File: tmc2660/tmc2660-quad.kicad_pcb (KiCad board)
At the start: 4 copper layers, 125 x 40 mm, 81 parts, among them J1 Power, J100 0R, J2 DataIn, J200 0R, J300 0R, J400 0R, M0 Mount, M1 Mount, M100 Mount, M101 Mount, M200 Mount, M201 Mount, M300 Mount, M301 Mount, M400 Mount, M401 Mount, P100 Motor, P200 Motor, P300 Motor, P400 Motor, U100 TMC2660, U200 TMC2660, U300 TMC2660, U400 TMC2660

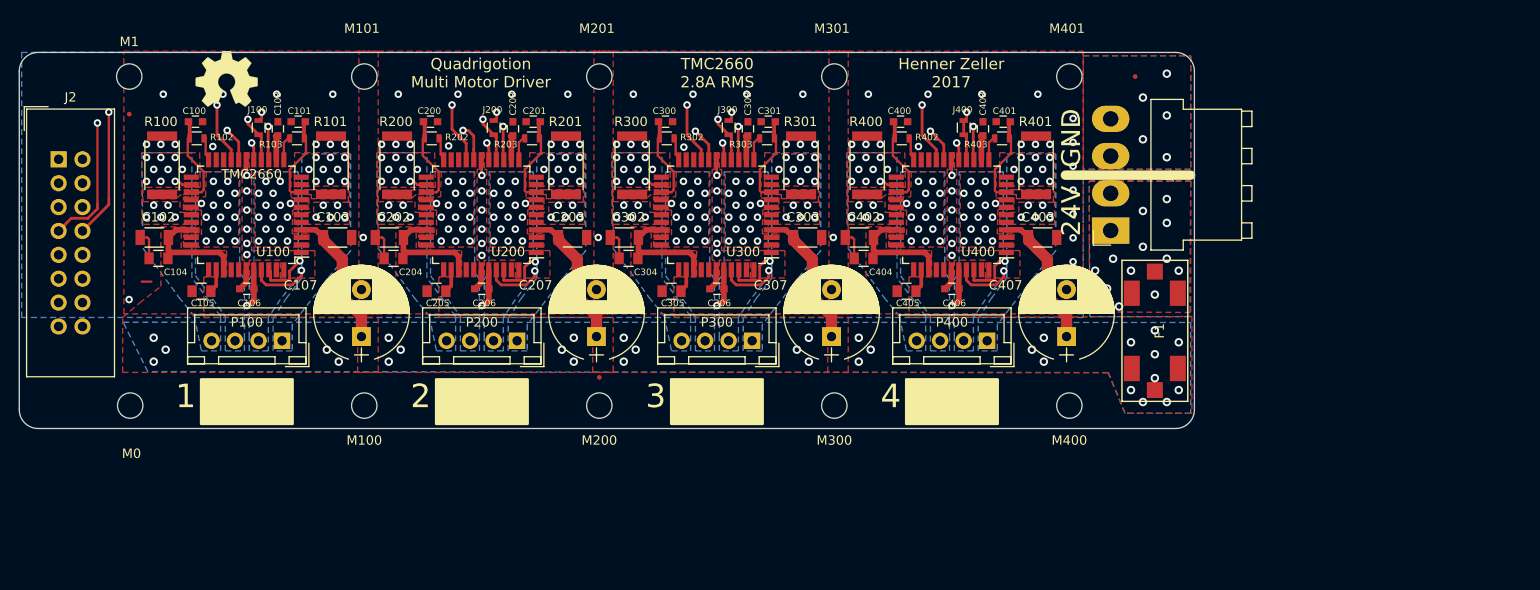
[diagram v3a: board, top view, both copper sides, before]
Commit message: Update tmc2660-quad with new template.
o Start out with a tmc2660-quad-baseline that is filled
  in with zones and tracks from the template.
o The separation from baseline and template allows faster
  updates later.
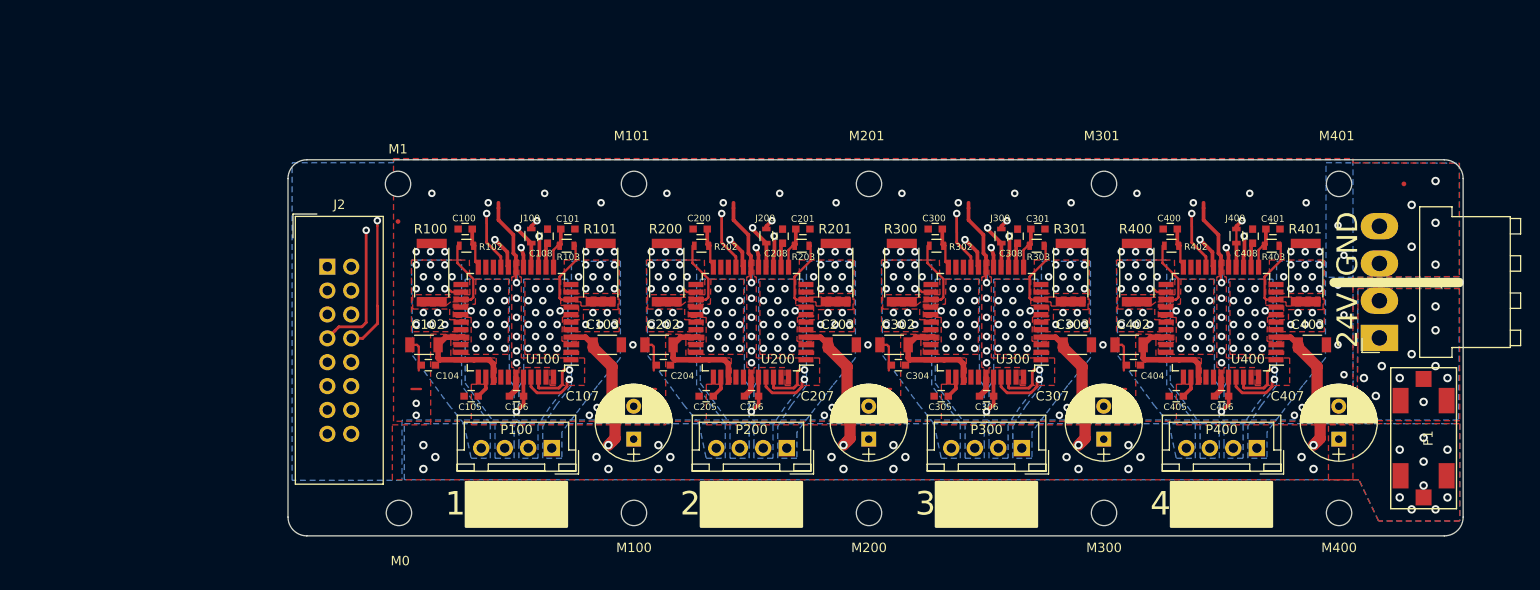
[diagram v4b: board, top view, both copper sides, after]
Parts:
- removed the REF** at (121.3, 83.1)
- removed REF***: OSHW-Symbol_6.7x6mm_SilkScreen, Symbols:OSHW-Symbol_6.7x6mm_SilkScreen
- C104, C105, C204, C205, C304, C305, C404, C405: footprint Capacitors_SMD:C_0805 -> Capacitors_SMD:C_0603
- C107, C207, C307, C407: value 100u -> 180u; footprint Capacitors_THT:CP_Radial_D10.0mm_P5.00mm -> Capacitors_THT:CP_Radial_D8.0mm_P3.50mm
- moved J100 31.2 mm to (114.1, 68.0)
- moved J200 31.2 mm to (139.1, 68.0)
- moved J300 31.2 mm to (164.1, 68.0)
- moved J400 31.2 mm to (189.1, 68.0)
- moved C107 30.9 mm to (125.0, 89.7)
- moved C207 30.9 mm to (150.0, 89.7)
- moved C307 30.9 mm to (175.0, 89.7)
- moved C407 30.9 mm to (200.0, 89.7)
- moved C103 30.9 mm to (122.2, 79.6)
- moved C106 30.9 mm to (112.5, 85.1)
- moved C206 30.9 mm to (137.5, 85.1)
- moved C306 30.9 mm to (162.5, 85.1)
- moved C402 30.9 mm to (177.7, 79.6)
- moved C406 30.9 mm to (187.5, 85.1)
- moved M100 30.9 mm to (125.0, 97.5)
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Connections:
- net Net-(C105-Pad2) renamed /TMC2660-100/VHS
- net Net-(C205-Pad2) renamed /TMC2660-200/VHS
- net Net-(C305-Pad2) renamed /TMC2660-300/VHS
- net Net-(C405-Pad2) renamed /TMC2660-400/VHS
- C100 pad 1: /TMC2660-100/BRB -> GND
- C100 pad 2: GND -> Net-(C100-Pad2)
- C101 pad 1: GND -> Net-(C101-Pad1)
- C101 pad 2: /TMC2660-100/BRA -> GND
- C200 pad 1: /TMC2660-200/BRB -> GND
- C200 pad 2: GND -> Net-(C200-Pad2)
- C201 pad 1: GND -> Net-(C201-Pad1)
- C201 pad 2: /TMC2660-200/BRA -> GND
- C300 pad 1: /TMC2660-300/BRB -> GND
- C300 pad 2: GND -> Net-(C300-Pad2)
- C301 pad 1: GND -> Net-(C301-Pad1)
- C301 pad 2: /TMC2660-300/BRA -> GND
- C400 pad 1: /TMC2660-400/BRB -> GND
- C400 pad 2: GND -> Net-(C400-Pad2)
- C401 pad 1: GND -> Net-(C401-Pad1)
- C401 pad 2: /TMC2660-400/BRA -> GND
- R102 pad 2: Net-(R102-Pad2) -> Net-(C100-Pad2)
- R103 pad 1: Net-(R103-Pad1) -> Net-(C101-Pad1)
- R202 pad 2: Net-(R202-Pad2) -> Net-(C200-Pad2)
- R203 pad 1: Net-(R203-Pad1) -> Net-(C201-Pad1)
- R302 pad 2: Net-(R302-Pad2) -> Net-(C300-Pad2)
- R303 pad 1: Net-(R303-Pad1) -> Net-(C301-Pad1)
- R402 pad 2: Net-(R402-Pad2) -> Net-(C400-Pad2)
- R403 pad 1: Net-(R403-Pad1) -> Net-(C401-Pad1)
- U100 pad 12: Net-(R103-Pad1) -> Net-(C101-Pad1)
- U100 pad 22: Net-(R102-Pad2) -> Net-(C100-Pad2)
- U200 pad 12: Net-(R203-Pad1) -> Net-(C201-Pad1)
- U200 pad 22: Net-(R202-Pad2) -> Net-(C200-Pad2)
- U300 pad 12: Net-(R303-Pad1) -> Net-(C301-Pad1)
- U300 pad 22: Net-(R302-Pad2) -> Net-(C300-Pad2)
- U400 pad 12: Net-(R403-Pad1) -> Net-(C401-Pad1)
- U400 pad 22: Net-(R402-Pad2) -> Net-(C400-Pad2)
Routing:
- net GND: track 39.3 -> 71.2 mm, vias 102 -> 98
- net GLOBAL_MOSI: track 113.7 -> 129.7 mm
- net SCLK: track 106.4 -> 121.0 mm
- net ~ENABLE: track 123.2 -> 133.6 mm
- net CS: track 114.9 -> 124.7 mm
- net Net-(C401-Pad1): track 0.00 -> 4.59 mm
- net Net-(C301-Pad1): track 0.00 -> 4.59 mm
- net Net-(C201-Pad1): track 0.00 -> 4.59 mm
- net Net-(C101-Pad1): track 0.00 -> 4.59 mm
- net Net-(C400-Pad2): track 0.00 -> 4.54 mm
- net Net-(C300-Pad2): track 0.00 -> 4.54 mm
- net Net-(C200-Pad2): track 0.00 -> 4.54 mm
- net Net-(C100-Pad2): track 0.00 -> 4.54 mm
- net Net-(R403-Pad1): track 2.76 -> 0.00 mm
- net Net-(R303-Pad1): track 2.76 -> 0.00 mm
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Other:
- net class Default: clearance 0.18 -> 0.21
- rule trace_clearance: 0.18 -> 0.21
- board text removed: "%%gitversion%%"
- board text removed: "Henner Zeller 2017"
- board text removed: "Quadrigotion Multi Motor Driver"
- board text removed: "TMC2660 2.8A RMS"
- board text removed: "github.com/hzeller/quadrigotion"

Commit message: Add bottom silkscreen.
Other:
- board text added: "%%gitversion%%"
- board text added: "http://quadrigotion.org/"
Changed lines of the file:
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@@
   (general
     (thickness 1.6)
-    (drawings 33)
+    (drawings 35)
     (tracks 1096)
     (zones 0)
@@
     )
   )
+  (gr_text http://quadrigotion.org/ (at 198.3645 94.732) (layer B.SilkS)
+    (effects (font (size 1.2 1.2) (thickness 0.2)) (justify left mirror))
+  )
+  (gr_text %%gitversion%% (at 112.5125 94.732) (layer B.SilkS)
+    (effects (font (size 1.2 1.2) (thickness 0.2)) (justify mirror))
+  )
   (gr_text 4 (at 182.0945 96.51) (layer F.SilkS)

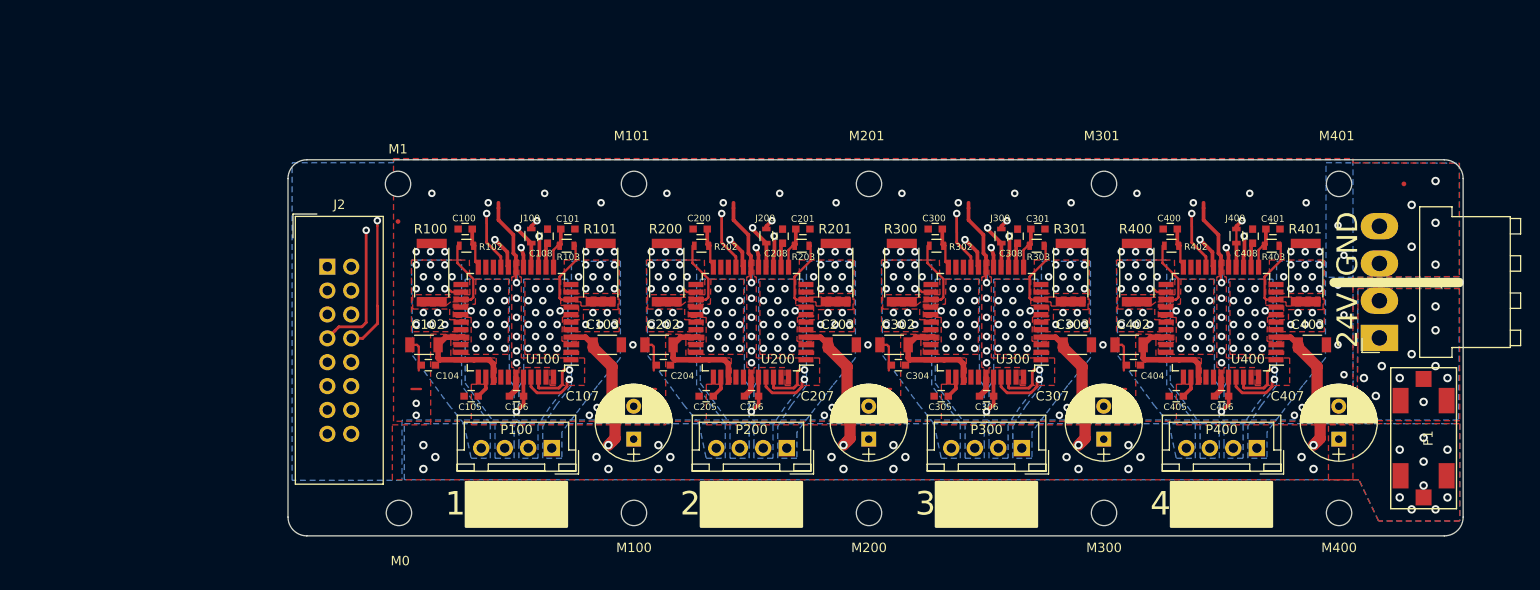
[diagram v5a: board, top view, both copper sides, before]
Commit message: Add front silkscreen. Re-add center fiducial.
o Front silkscreen and center fiducial got lost in the previous
  steps.
o Re-add in the baseline file and re-generate the final file.
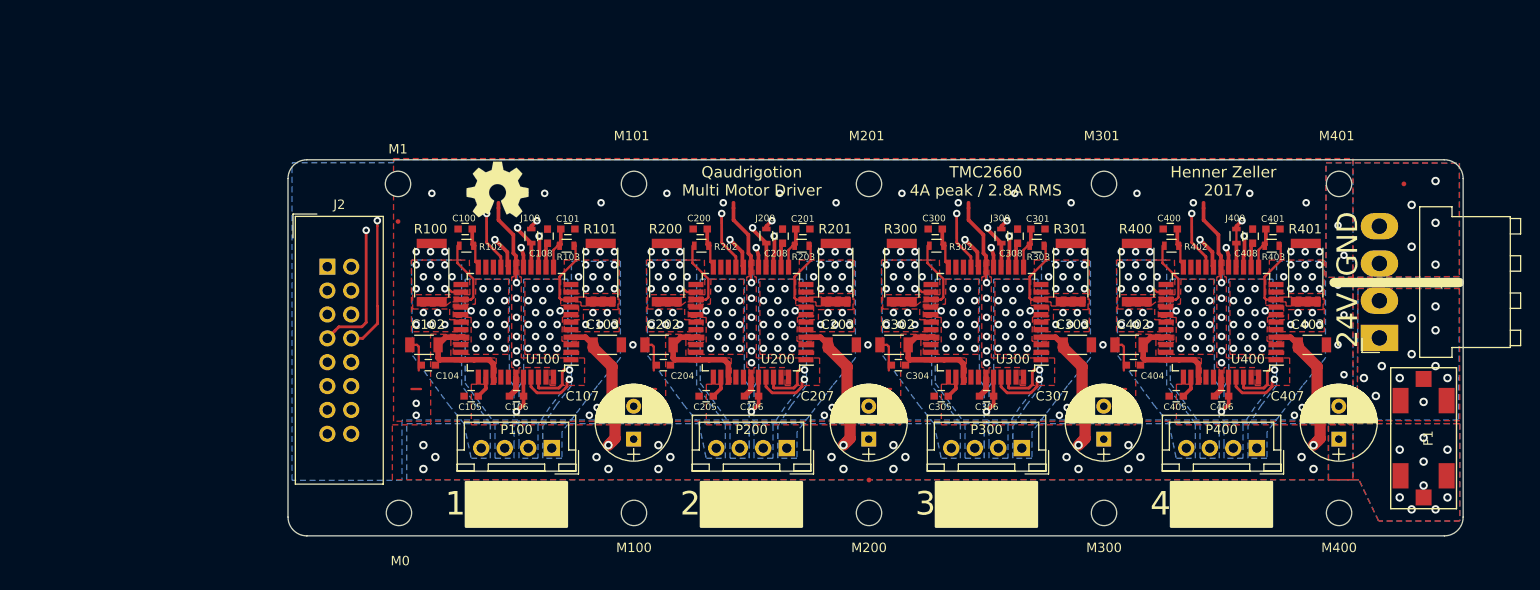
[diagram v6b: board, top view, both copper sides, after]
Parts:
- added REF**: Fiducial_0.5mm_Dia_1mm_Outer, Fiducials:Fiducial_0.5mm_Dia_1mm_Outer, F.Cu at (150.0, 94.0)
- added REF***: OSHW-Symbol_6.7x6mm_SilkScreen, Symbols:OSHW-Symbol_6.7x6mm_SilkScreen, F.Cu at (110.5, 63.1)
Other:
- board text added: "Henner Zeller 2017"
- board text added: "Qaudrigotion Multi Motor Driver"
- board text added: "TMC2660 4A peak / 2.8A RMS"

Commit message: Merge new template + baseline.
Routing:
- net DIR4: track 110.4 -> 111.0 mm
